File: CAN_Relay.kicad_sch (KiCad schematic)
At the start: 29 parts, among them IC1 REG1117-5, J1 430450601, J2 BCS-114-L-S-PE-BE, J3 BCS-114-L-S-PE-BE, J4 691305340008, J5 691305340008, U2 BTS716GB, U3 BTS716GB, U4 ADM3057EBRWZ

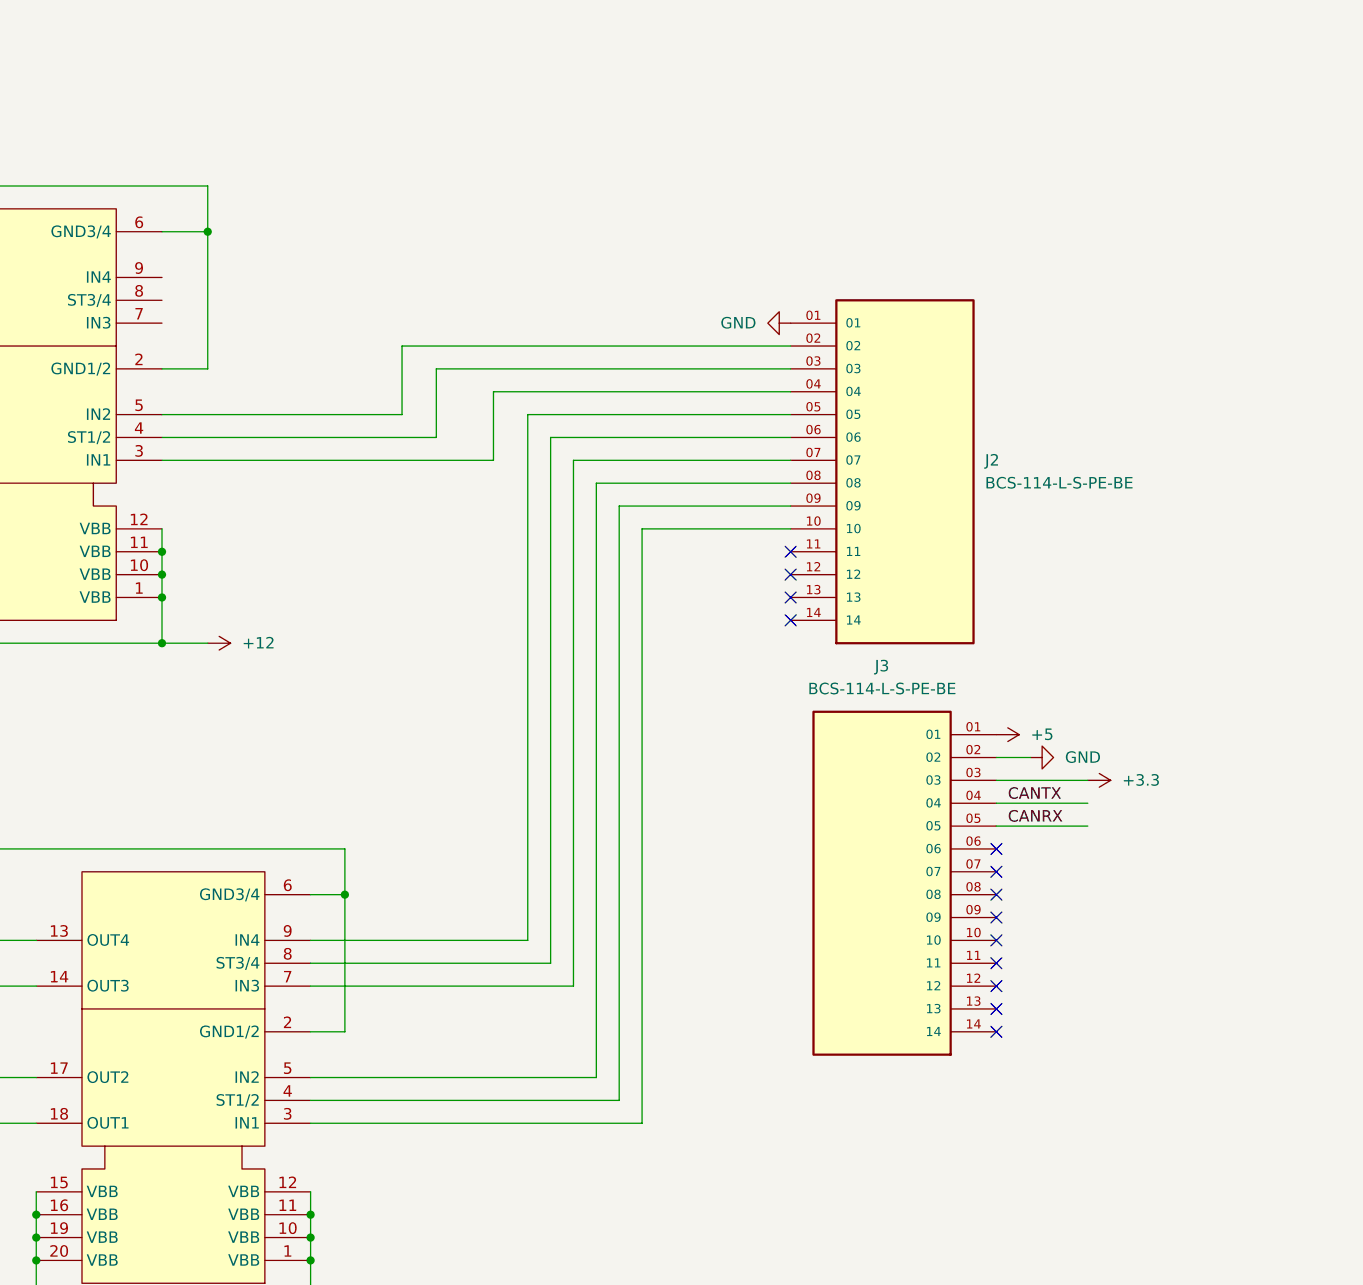
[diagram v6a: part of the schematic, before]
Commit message: Redid layout to make board more compact
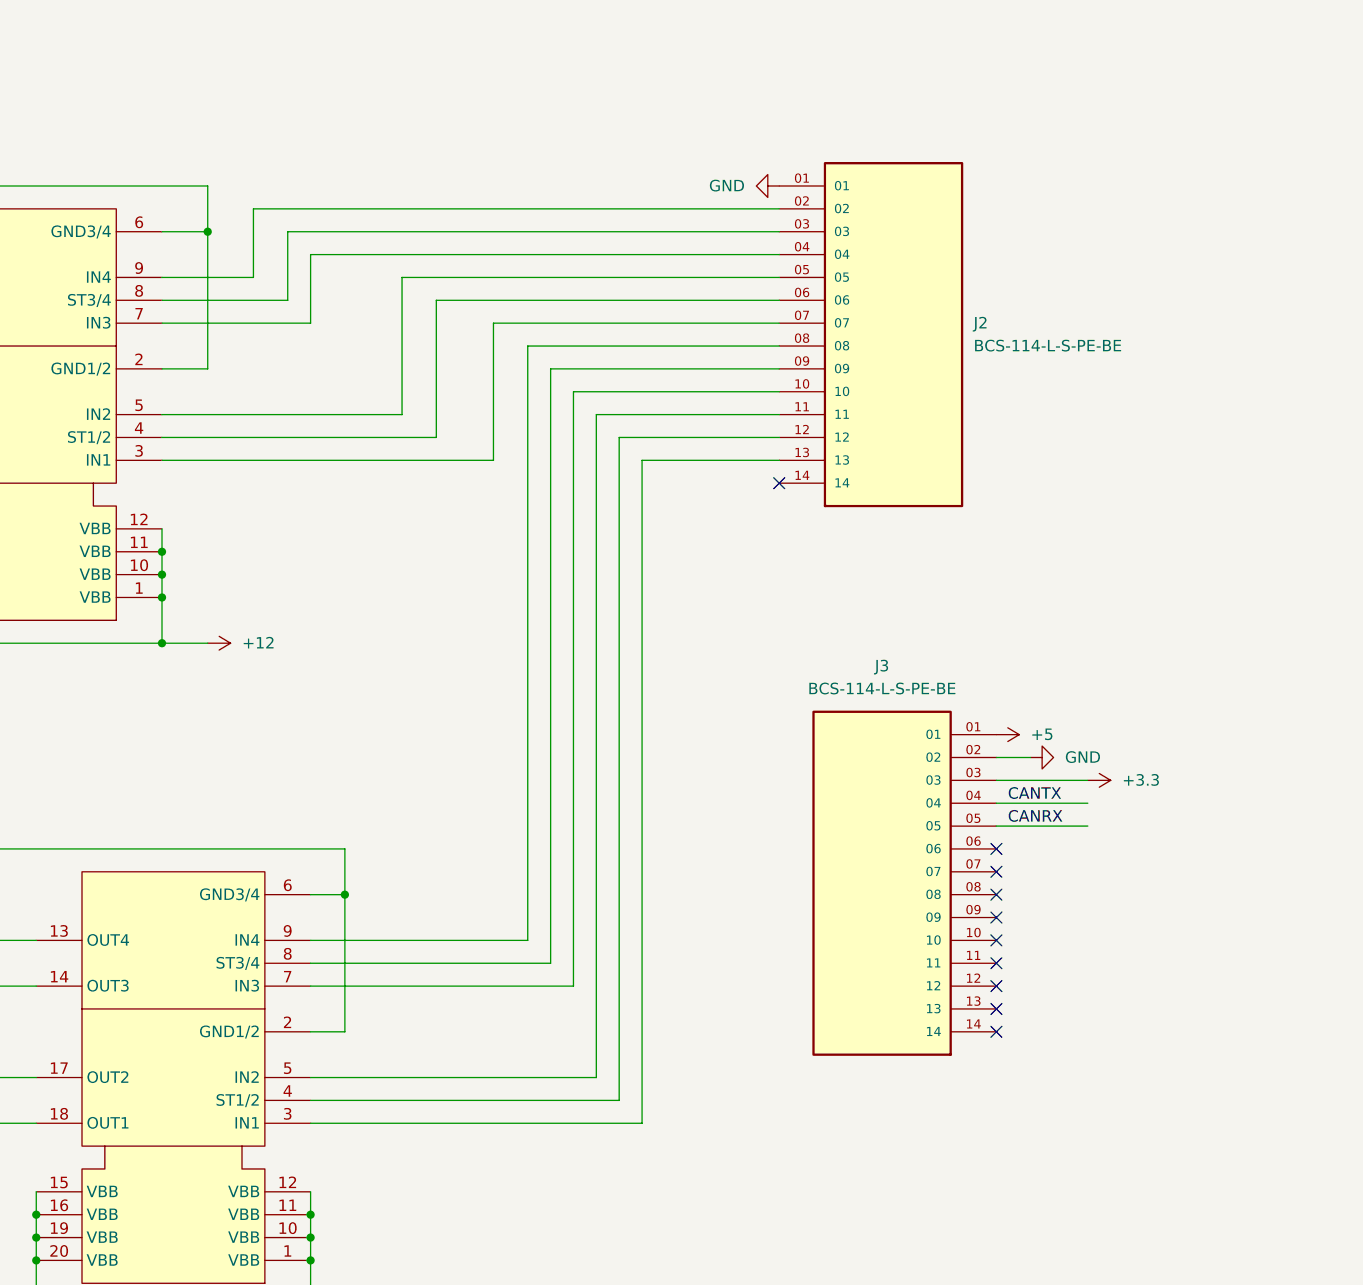
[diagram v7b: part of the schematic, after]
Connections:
- net at U3.3 (IN1): now also J2.13; no longer J2.10
- net at U3.4 (ST1/2): now also J2.12; no longer J2.09
- net at U3.5 (IN2): now also J2.11; no longer J2.08
- net at U3.7 (IN3): now also J2.10; no longer J2.07
- net at U3.8 (ST3/4): now also J2.09; no longer J2.06
- net at U3.9 (IN4): now also J2.08; no longer J2.05
- net at J2.02: now also U2.9 (IN4); no longer U2.5 (IN2)
- net at J2.03: now also U2.8 (ST3/4); no longer U2.4 (ST1/2)
- net at J2.04: now also U2.7 (IN3); no longer U2.3 (IN1)
- new net: J2.05, U2.5 (IN2)
- new net: J2.06, U2.4 (ST1/2)
- new net: J2.07, U2.3 (IN1)
- no-connect marks 47 -> 44
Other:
- moved on the sheet: J2
